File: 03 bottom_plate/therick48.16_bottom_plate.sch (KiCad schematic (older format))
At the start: 88 parts, among them U1 HOLE, U10 HOLE, U11 HOLE, U12 HOLE, U13 HOLE, U14 HOLE, U15 HOLE, U16 HOLE, U17 HOLE, U18 HOLE, U19 HOLE, U2 HOLE, U20 HOLE, U21 HOLE, U22 HOLE, U23 HOLE, U24 HOLE, U25 HOLE, U26 HOLE, U27 HOLE, U28 HOLE, U29 HOLE, U3 HOLE, U30 HOLE, U31 HOLE, U32 HOLE, U33 HOLE, U34 HOLE, U35 HOLE, U36 HOLE, U37 HOLE, U38 HOLE, U39 HOLE, U4 HOLE, U40 HOLE, U41 HOLE, U42 HOLE, U43 HOLE, U44 HOLE, U45 HOLE, U46 HOLE, U47 HOLE, U48 HOLE, U49 HOLE, U5 HOLE, U50 HOLE, U51 HOLE, U52 HOLE, U53 HOLE, U54 HOLE, U55 HOLE, U56 HOLE, U57 HOLE, U58 HOLE, U59 HOLE, U6 HOLE, U60 HOLE, U61 HOLE, U62 HOLE, U63 HOLE, U64 HOLE, U65 HOLE, U66 HOLE, U67 HOLE, U68 HOLE, U69 HOLE, U7 HOLE, U70 HOLE, U8 HOLE, U9 HOLE

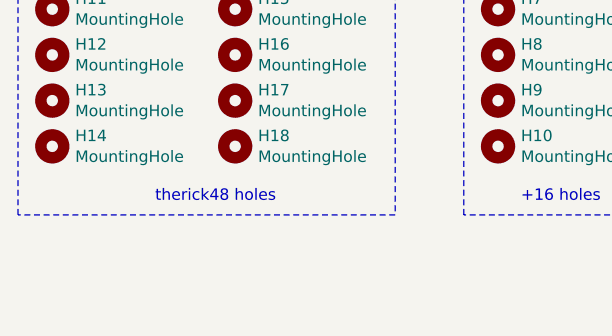
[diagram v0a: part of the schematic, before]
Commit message: Add reset hole to bottom plate
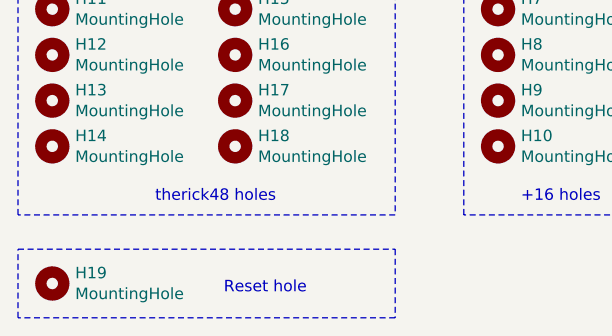
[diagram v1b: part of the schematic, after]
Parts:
- added H19: MountingHole, random-keyboard-parts:Generic-Mounthole, symbol Mechanical:MountingHole
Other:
- note added: "Reset hole"
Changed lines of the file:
@@
 EESchema Schematic File Version 4
-LIBS:therick64BA_bottom_plate-cache
+LIBS:therick48.16_bottom_plate-cache
 EELAYER 29 0
 EELAYER END
@@
 Wire Notes Line
 	3550 5100 3550 4050
+$Comp
+L Mechanical:MountingHole H19
+U 1 1 5ECA8D8E
+P 1750 5400
+F 0 "H19" H 1850 5446 50  0000 L CNN
+F 1 "MountingHole" H 1850 5355 50  0000 L CNN
+F 2 "random-keyboard-parts:Generic-Mounthole" H 1750 5400 50  0001 C CNN
+F 3 "~" H 1750 5400 50  0001 C CNN
+	1    1750 5400
+	1    0    0    -1
+$EndComp
+Text Notes 2500 5450 0    50   ~ 0
+Reset hole
+Wire Notes Line
+	1600 5250 3250 5250
+Wire Notes Line
+	3250 5250 3250 5550
+Wire Notes Line
+	3250 5550 1600 5550
+Wire Notes Line
+	1600 5550 1600 5250
 $EndSCHEMATC
